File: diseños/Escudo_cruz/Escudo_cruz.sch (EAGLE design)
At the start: 7 parts, among them J1 1X2-3.5MM, X1 TERMINAL-BLOCK-3.5MM-4-PIN-RO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

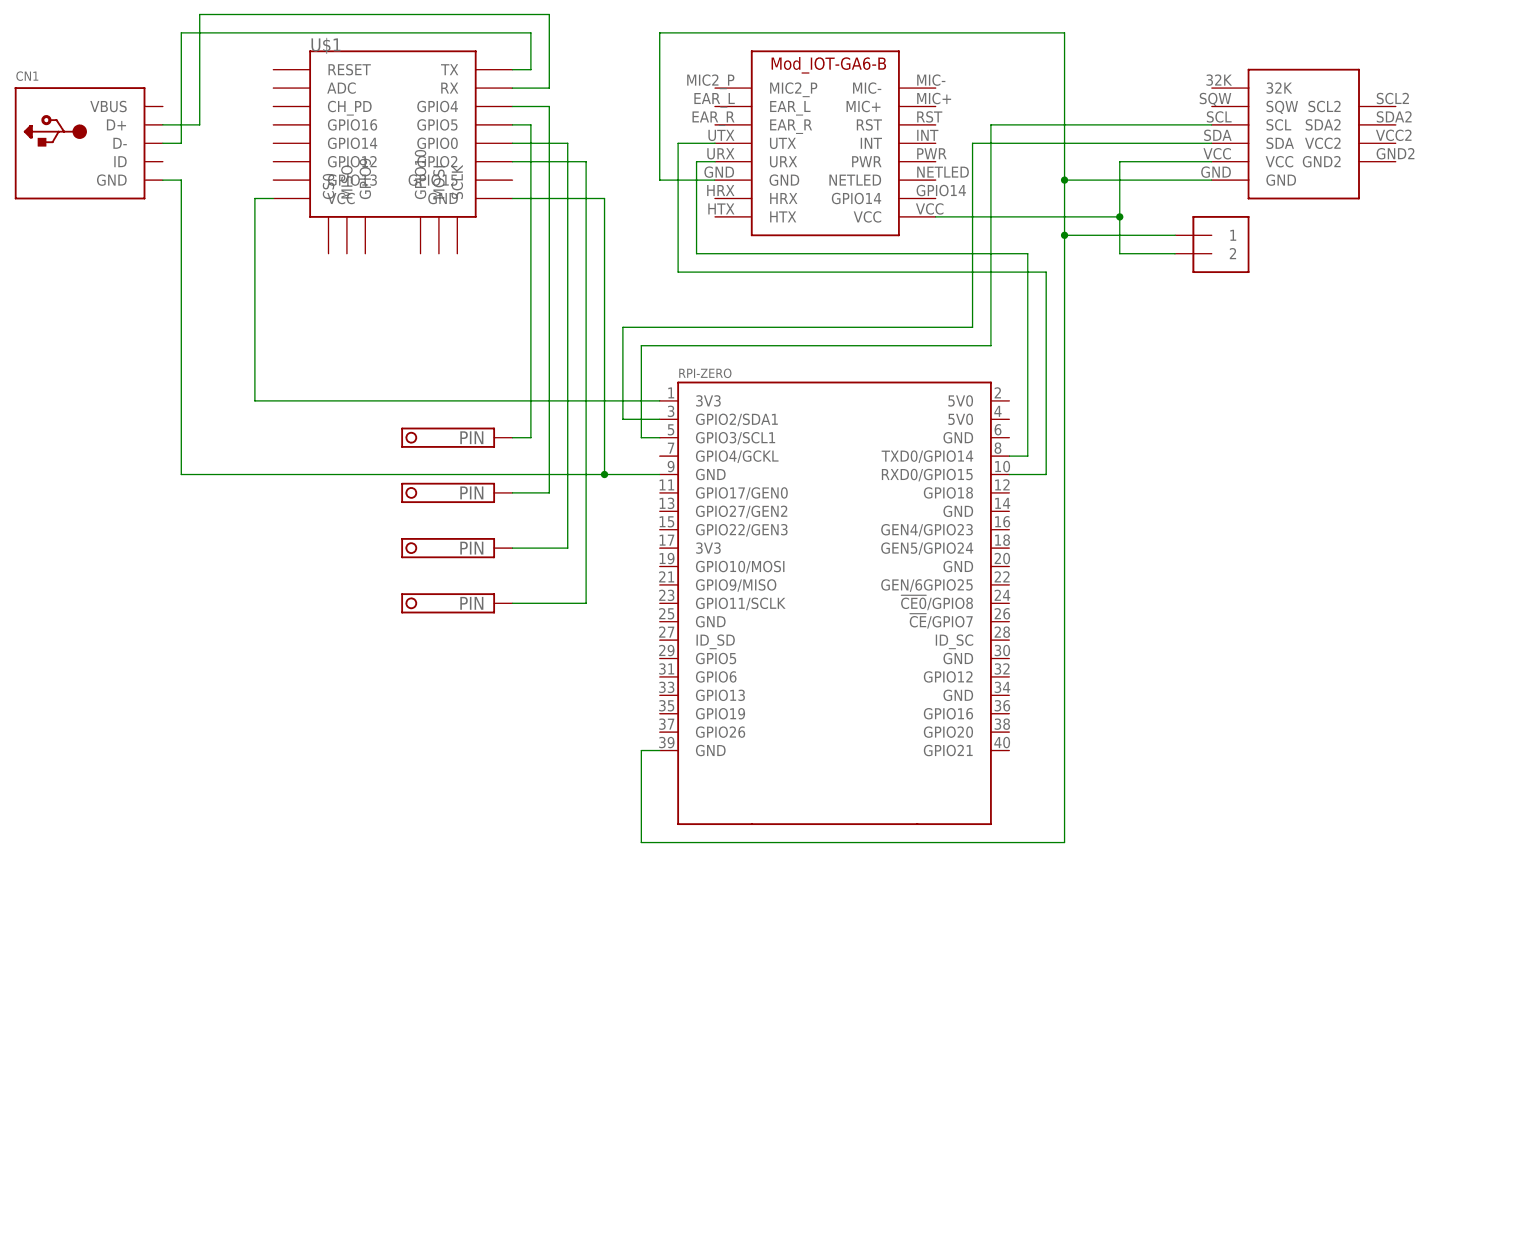
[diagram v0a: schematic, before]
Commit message: Se agrega ESP para comunicarse mediante I2C con Raspberry
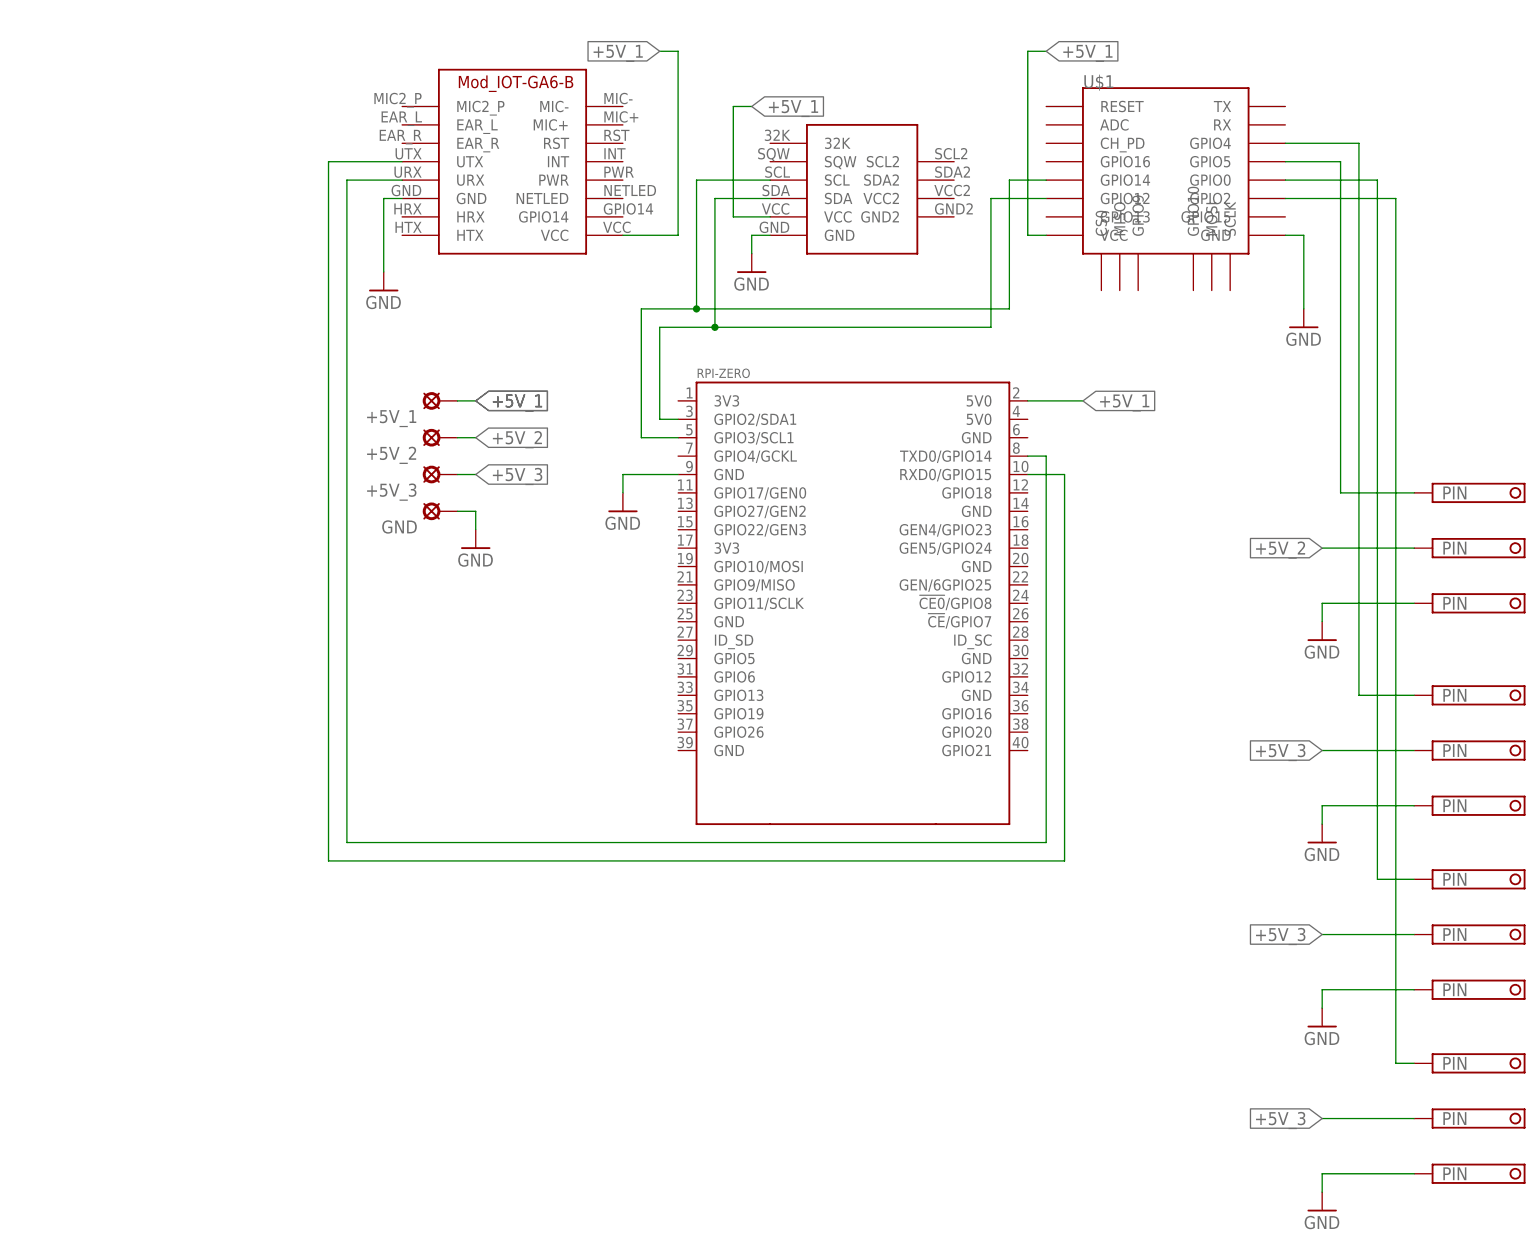
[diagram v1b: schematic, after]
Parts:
- removed CN1: (no value), adafruit:USBMINIB
- removed J1: 1X2-3.5MM, adafruit:1X2-3.5MM
- added +5V_1, +5V_2, +5V_3, GND: LSP10, solpad:LSP10
- added X2, X3, X4: TERMINAL-BLOCK-3.5MM-3-PIN-ROUND-PAD, Rembrandt Electronics - Terminal Block 3-5mm v1-0:TERMINAL-BLOCK-3.5MM-3-PIN-ROUND-PAD
- X1: value TERMINAL-BLOCK-3.5MM-4-PIN-ROUND-PAD -> TERMINAL-BLOCK-3.5MM-3-PIN-ROUND-PAD; device Rembrandt Electronics - Terminal Block 3-5mm v1-0:TERMINAL-BLOCK-3.5MM-4-PIN-ROUND-PAD -> Rembrandt Electronics - Terminal Block 3-5mm v1-0:TERMINAL-BLOCK-3.5MM-3-PIN-ROUND-PAD
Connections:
- removed net 3V3@1: U$1.VCC, U$2.3V3@1
- removed net GND@3: J1.1, U$2.GND@3, U$3.GND, U$4.GND
- removed net N$1 (its old number): J1.2, U$3.VCC, U$4.VCC
- removed net N$10: CN1.D-, U$1.TX
- removed net N$11: CN1.D+, U$1.RX
- removed net N$7 (its old number): U$1.GPIO4, X1-2.VCC
- removed net N$8: U$1.GPIO0, X1-3.VCC
- removed net N$9: U$1.GPIO2, X1-4.VCC
- new net +5V_1: +5V_1.MP, U$1.VCC, U$2.5V0@1, U$3.VCC, U$4.VCC
- new net +5V_2: +5V_2.MP, X1-2.VCC
- new net +5V_3: +5V_3.MP, X2-2.VCC, X3-2.VCC, X4-2.VCC
- new net GND: GND.MP, U$1.GND, U$3.GND, U$4.GND, X1-3.VCC, X2-3.VCC, X3-3.VCC, X4-3.VCC
- new net N$12: U$1.GPIO4, X2-1.VCC
- new net N$13: U$1.GPIO0, X3-1.VCC
- new net N$14: U$1.GPIO2, X4-1.VCC
- net GND@1: no longer CN1.GND, U$1.GND
- net N$3: now also U$1.GPIO12
- net N$4: now also U$1.GPIO14
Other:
- moved on the sheet: U$1
